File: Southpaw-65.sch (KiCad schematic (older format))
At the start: 14 parts

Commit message: Leftpad and top row added
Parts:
- removed U?: ATmega32U4-AU, Package_QFP:TQFP-44_10x10mm_P0.8mm, symbol MCU_Microchip_ATmega:ATmega32U4-AU
- added C?: 1uF, symbol Device:C_Small
- added D? (x35): SOD-123, symbol Device:D_Small
- added J?: USB_C_Receptacle_USB2.0, symbol Connector:USB_C_Receptacle_USB2.0
- added MX? (x35): MX-NoLED, symbol MX_Alps_Hybrid:MX-NoLED
- added R? (x2): 5k1, symbol Device:R_Small
- added U?: ATmega32U4-AU, Package_QFP:TQFP-44_10x10mm_P0.8mm, symbol MCU_Microchip_ATmega:ATmega32U4-AU
- C?: value C_Small -> 1uF
- C? (x3): value 0.1uF -> 100nF
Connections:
- net +5V: now also C?.1, J?.A4 (VBUS), J?.A9 (VBUS), J?.B4 (VBUS), J?.B9 (VBUS), U?.14 (VCC), U?.2 (UVCC), U?.24 (AVCC), U?.34 (VCC), U?.44 (AVCC), U?.7 (VBUS)
- net D+: now also J?.A6 (D+), J?.B6 (D+)
- net D-: now also J?.A7 (D-), J?.B7 (D-)
- net GND: now also C?.2, J?.A1 (GND), J?.A12 (GND), J?.B1 (GND), J?.B12 (GND), J?.S1 (SHIELD), R?.1, R?.1, U?.15 (GND), U?.23 (GND), U?.35 (GND), U?.43 (GND), U?.5 (UGND)
- net Reset: now reaches R?.2, SW?.2
- net Reset: now also U?.13 (~RESET)
- net C16: now reaches C?.1, Y?.3
- net C16: now also U?.16 (XTAL2)
- net C17: now reaches C?.1, Y?.1
- net C17: now also U?.17 (XTAL1)
- net at R?.1: now also U?.3 (D-)
- net at R?.2: now also U?.33 (~HWB~/PE2)
- net at R?.1: now also U?.4 (D+)
- net at C?.1: now also U?.6 (UCAP)
- new net: J?.A5 (CC1), R?.2
- new net: J?.B5 (CC2), R?.2
- new net: D?.2 (A), MX?.2 (ROW) (x35)
- new net COL0: MX?.1 (COL), MX?.1 (COL), MX?.1 (COL), MX?.1 (COL), MX?.1 (COL)
- new net COL1: MX?.1 (COL), MX?.1 (COL), MX?.1 (COL), MX?.1 (COL), MX?.1 (COL)
- new net COL2: MX?.1 (COL), MX?.1 (COL), MX?.1 (COL), MX?.1 (COL), MX?.1 (COL)
- new net COL3: MX?.1 (COL), MX?.1 (COL), MX?.1 (COL), MX?.1 (COL), MX?.1 (COL)
- new net ROW0: D?.1 (K), D?.1 (K), D?.1 (K), D?.1 (K)
- new net ROW1: D?.1 (K), D?.1 (K), D?.1 (K), D?.1 (K)
- new net ROW2: D?.1 (K), D?.1 (K), D?.1 (K), D?.1 (K)
- new net ROW3: D?.1 (K), D?.1 (K), D?.1 (K), D?.1 (K)
- new net ROW4: D?.1 (K), D?.1 (K), D?.1 (K), D?.1 (K)
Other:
- note added: "Crystal Jade"
- note added: "MCU\n"
- note added: "Reset"
- note added: "USB C"
- moved on the sheet: C?, R?, SW?, Y?

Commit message: Finished switch matrix
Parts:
- removed D?: SOD-123, symbol Device:D_Small
- removed MX?: MX-NoLED, symbol MX_Alps_Hybrid:MX-NoLED
- added D? (x59): SOD-123, symbol Device:D_Small
- added MX? (x59): MX-NoLED, symbol MX_Alps_Hybrid:MX-NoLED
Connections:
- net ROW0: now also D?.1 (K), D?.1 (K), D?.1 (K), D?.1 (K), D?.1 (K), D?.1 (K), D?.1 (K), D?.1 (K), D?.1 (K), D?.1 (K), D?.1 (K), D?.1 (K), D?.1 (K), D?.1 (K), D?.1 (K), D?.1 (K)
- net ROW4: now also D?.1 (K), D?.1 (K), D?.1 (K), D?.1 (K), D?.1 (K), D?.1 (K), D?.1 (K), D?.1 (K), D?.1 (K), D?.1 (K), D?.1 (K)
- net COL4: now reaches MX?.1 (COL)
- net COL4: now also MX?.1 (COL), MX?.1 (COL), MX?.1 (COL), MX?.1 (COL)
- net COL5: now reaches MX?.1 (COL)
- net COL5: now also MX?.1 (COL), MX?.1 (COL), MX?.1 (COL), MX?.1 (COL)
- net COL6: now reaches MX?.1 (COL)
- net COL6: now also MX?.1 (COL), MX?.1 (COL), MX?.1 (COL), MX?.1 (COL)
- net COL7: now reaches MX?.1 (COL)
- net COL7: now also MX?.1 (COL), MX?.1 (COL), MX?.1 (COL)
- net COL8: now reaches MX?.1 (COL)
- net COL8: now also MX?.1 (COL), MX?.1 (COL), MX?.1 (COL), MX?.1 (COL)
- net COL9: now reaches MX?.1 (COL)
- net COL9: now also MX?.1 (COL), MX?.1 (COL), MX?.1 (COL), MX?.1 (COL)
- net COL10: now reaches MX?.1 (COL)
- net COL10: now also MX?.1 (COL), MX?.1 (COL), MX?.1 (COL), MX?.1 (COL)
- net COL11: now reaches MX?.1 (COL)
- net COL11: now also MX?.1 (COL), MX?.1 (COL), MX?.1 (COL)
- net COL12: now reaches MX?.1 (COL)
- net COL12: now also MX?.1 (COL), MX?.1 (COL), MX?.1 (COL)
- net COL13: now reaches MX?.1 (COL)
- net COL13: now also MX?.1 (COL), MX?.1 (COL), MX?.1 (COL), MX?.1 (COL)
- net COL14: now reaches MX?.1 (COL)
- net COL14: now also MX?.1 (COL), MX?.1 (COL), MX?.1 (COL), MX?.1 (COL)
- net COL15: now reaches MX?.1 (COL)
- net COL15: now also MX?.1 (COL), MX?.1 (COL), MX?.1 (COL)
- net COL17: now reaches MX?.1 (COL)
- net COL17: now also MX?.1 (COL)
- net COL18: now reaches MX?.1 (COL)
- net COL18: now also MX?.1 (COL), MX?.1 (COL), MX?.1 (COL)
- new net: D?.2 (A), MX?.2 (ROW) (x59)
- new net: D?.1 (K), D?.1 (K), D?.1 (K), D?.1 (K), D?.1 (K), D?.1 (K), D?.1 (K), D?.1 (K), D?.1 (K), D?.1 (K), D?.1 (K), D?.1 (K), D?.1 (K), D?.1 (K), D?.1 (K), D?.1 (K)
- new net: D?.1 (K), D?.1 (K), D?.1 (K), D?.1 (K), D?.1 (K), D?.1 (K), D?.1 (K), D?.1 (K), D?.1 (K), D?.1 (K), D?.1 (K), D?.1 (K), D?.1 (K), D?.1 (K), D?.1 (K) (x2)
- new net COL16: MX?.1 (COL), MX?.1 (COL), MX?.1 (COL), MX?.1 (COL), MX?.1 (COL)
- new net COL19: MX?.1 (COL), MX?.1 (COL), MX?.1 (COL), MX?.1 (COL)
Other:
- moved on the sheet: D?, MX?

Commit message: Redid matrix
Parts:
- gave numbers to parts that had none: 204
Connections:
- net COL18: now also MX4-18.1 (COL)
- net COL19: now also MX4-19.1 (COL)
- net ROW1: now also D25.1 (K), D26.1 (K), D27.1 (K), D28.1 (K), D29.1 (K), D30.1 (K), D31.1 (K), D32.1 (K), D33.1 (K), D34.1 (K), D35.1 (K), D36.1 (K), D37.1 (K), D38.1 (K), D39.1 (K), D40.1 (K)
- net ROW2: now also D45.1 (K), D46.1 (K), D47.1 (K), D48.1 (K), D49.1 (K), D50.1 (K), D51.1 (K), D52.1 (K), D53.1 (K), D54.1 (K), D55.1 (K), D56.1 (K), D57.1 (K), D58.1 (K), D59.1 (K)
- net ROW3: now also D64.1 (K), D65.1 (K), D66.1 (K), D67.1 (K), D68.1 (K), D69.1 (K), D70.1 (K), D71.1 (K), D72.1 (K), D73.1 (K), D74.1 (K), D75.1 (K), D76.1 (K), D77.1 (K), D78.1 (K)

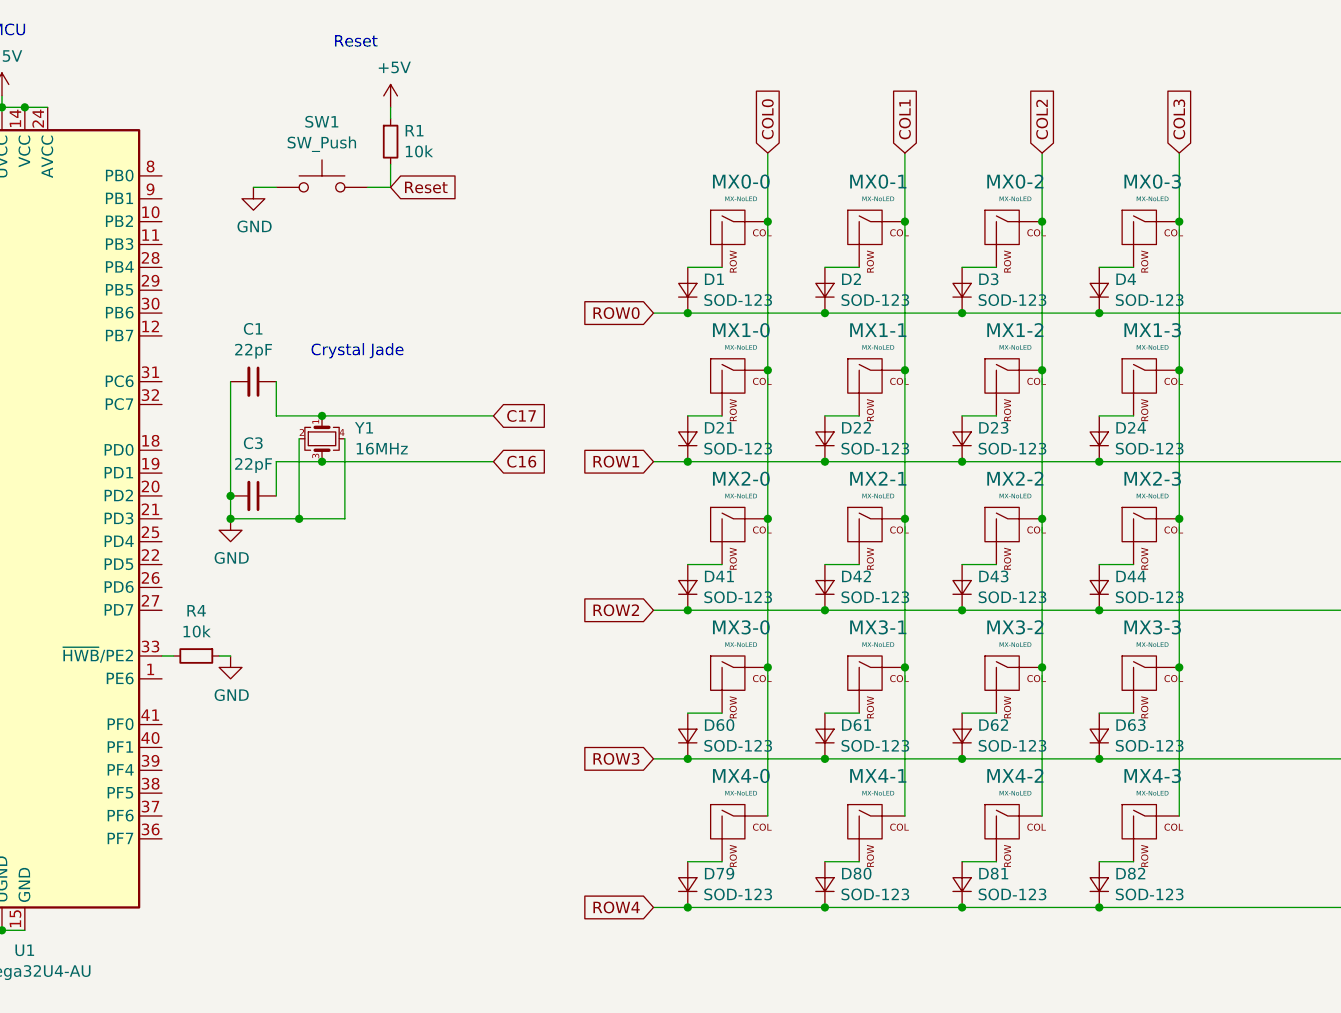
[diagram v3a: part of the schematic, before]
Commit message: Connected Matrix to Atmega
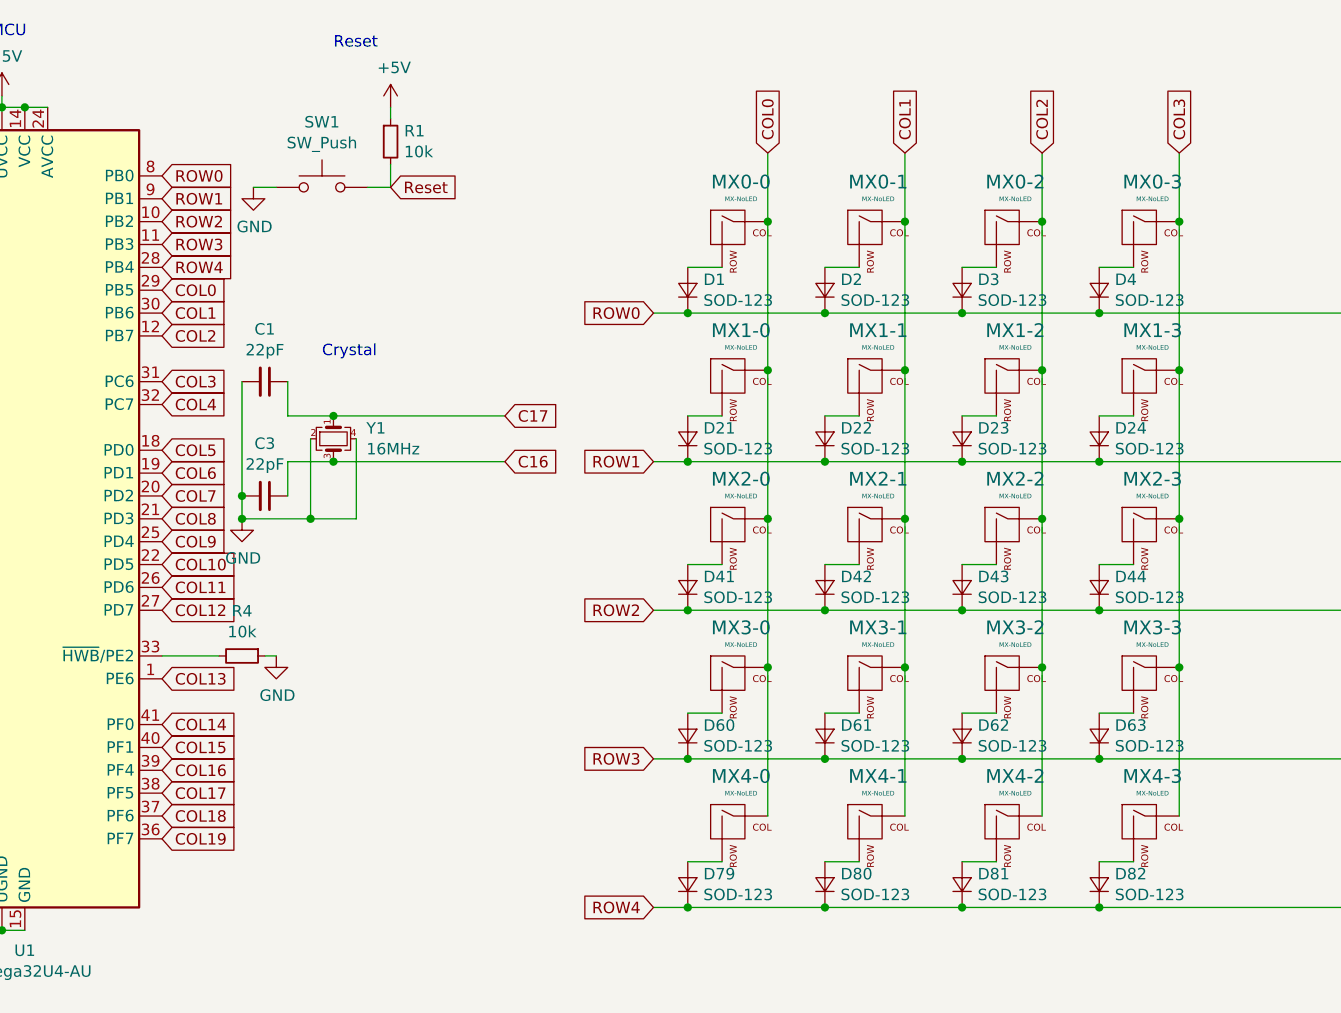
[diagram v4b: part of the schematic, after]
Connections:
- net COL0: now also U1.29 (PB5)
- net COL1: now also U1.30 (PB6)
- net COL10: now also U1.22 (PD5)
- net COL11: now also U1.26 (PD6)
- net COL12: now also U1.27 (PD7)
- net COL13: now also U1.1 (PE6)
- net COL14: now also U1.41 (PF0)
- net COL15: now also U1.40 (PF1)
- net COL16: now also U1.39 (PF4)
- net COL17: now also U1.38 (PF5)
- net COL18: now also U1.37 (PF6)
- net COL19: now also U1.36 (PF7)
- net COL2: now also U1.12 (PB7)
- net COL3: now also U1.31 (PC6)
- net COL4: now also U1.32 (PC7)
- net COL5: now also U1.18 (PD0)
- net COL6: now also U1.19 (PD1)
- net COL7: now also U1.20 (PD2)
- net COL8: now also U1.21 (PD3)
- net COL9: now also U1.25 (PD4)
- net ROW0: now also U1.8 (PB0)
- net ROW1: now also U1.9 (PB1)
- net ROW2: now also U1.10 (PB2)
- net ROW3: now also U1.11 (PB3)
- net ROW4: now also U1.28 (PB4)
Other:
- note added: "Crystal"
- note removed: "Crystal Jade"
- moved on the sheet: C1, C3, R4, Y1

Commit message: Set footprints for everything but switches and capcitators
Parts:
- D1, D10, D11, D12, D13, D14, D15, D16, D17, D18, D19, D2, D20, D21, D22, D23, D24, D25, D26, D27, D28, D29, D3, D30, D31, D32, D33, D34, D35, D36, D37, D38, D39, D4, D40, D41, D42, D43, D44, D45, D46, D47, D48, D49, D5, D50, D51, D52, D53, D54, D55, D56, D57, D58, D59, D6, D60, D61, D62, D63, D64, D65, D66, D67, D68, D69, D7, D70, D71, D72, D73, D74, D75, D76, D77, D78, D79, D8, D80, D81, D82, D83, D84, D85, D86, D87, D88, D89, D9, D90, D91, D92, D93: footprint (none) -> Diode_THT:D_DO-41_SOD81_P7.62mm_Horizontal
- J1: footprint (none) -> Connector_USB:USB_C_Receptacle_GCT_USB4085
- R1, R2, R3, R4, R5, R6: footprint (none) -> Resistor_THT:R_Axial_DIN0207_L6.3mm_D2.5mm_P7.62mm_Horizontal
- SW1: footprint (none) -> random-keyboard-parts:PushButton_6x6mm_TH
- Y1: footprint (none) -> Crystal:Crystal_HC49-U_Vertical

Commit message: Set keys
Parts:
- removed C2: 1uF, symbol Device:C_Small
- removed D57, D76: SOD-123, Diode_THT:D_DO-41_SOD81_P7.62mm_Horizontal, symbol Device:D_Small
- removed MX2-16, MX3-16: MX-NoLED, symbol MX_Alps_Hybrid:MX-NoLED
- removed R4: 10k, Resistor_THT:R_Axial_DIN0207_L6.3mm_D2.5mm_P7.62mm_Horizontal, symbol Device:R_Small
- removed U1: ATmega32U4-AU, Package_QFP:TQFP-44_10x10mm_P0.8mm, symbol MCU_Microchip_ATmega:ATmega32U4-AU
- added U1: ATmega32A-PU, Package_DIP:DIP-40_W15.24mm, symbol MCU_Microchip_ATmega:ATmega32A-PU
- MX0-0, MX0-1, MX0-10, MX0-11, MX0-12, MX0-13, MX0-14, MX0-15, MX0-16, MX0-17, MX0-18, MX0-19, MX0-2, MX0-3, MX0-4, MX0-5, MX0-6, MX0-7, MX0-8, MX0-9, MX1-0, MX1-1, MX1-10, MX1-11, MX1-12, MX1-13, MX1-14, MX1-15, MX1-16, MX1-17, MX1-19, MX1-2, MX1-3, MX1-5, MX1-6, MX1-7, MX1-8, MX1-9, MX2-0, MX2-1, MX2-10, MX2-11, MX2-12, MX2-13, MX2-14, MX2-15, MX2-19, MX2-2, MX2-3, MX2-5, MX2-6, MX2-7, MX2-8, MX2-9, MX3-0, MX3-1, MX3-10, MX3-11, MX3-12, MX3-13, MX3-14, MX3-18, MX3-19, MX3-2, MX3-3, MX3-5, MX3-6, MX3-7, MX3-8, MX3-9, MX4-0, MX4-1, MX4-14, MX4-16, MX4-18, MX4-19, MX4-2, MX4-3, MX4-5, MX4-9: footprint (none) -> MX_Alps_Hybrid:MX-1U
- MX1-18, MX1-4, MX4-4, MX4-6: footprint (none) -> MX_Alps_Hybrid:MX-1.5U
- MX2-18, MX3-4: footprint (none) -> MX_Alps_Hybrid:MX-2.25U
- MX2-4, MX3-15: footprint (none) -> MX_Alps_Hybrid:MX-1.75U
- MX4-10, MX4-8: footprint (none) -> MX_Alps_Hybrid:MX-2.75U
- MX4-13: footprint (none) -> MX_Alps_Hybrid:MX-1.25U
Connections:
- net +5V: now also U1.10 (VCC), U1.30 (AVCC)
- net C16: now also U1.12 (XTAL2)
- net C17: now also U1.13 (XTAL1)
- net COL0: now also U1.35 (PA5)
- net COL1: now also U1.34 (PA6)
- net COL10: now also U1.8 (PB7)
- net COL11: now also U1.22 (PC0)
- net COL12: now also U1.23 (PC1)
- net COL13: now also U1.24 (PC2)
- net COL14: now also U1.25 (PC3)
- net COL15: now also U1.26 (PC4)
- net COL16: now also U1.27 (PC5)
- net COL17: now also U1.28 (PC6)
- net COL18: now also U1.29 (PC7)
- net COL19: now also U1.14 (PD0)
- net COL2: now also U1.33 (PA7)
- net COL3: now also U1.1 (PB0)
- net COL4: now also U1.2 (PB1)
- net COL5: now also U1.3 (PB2)
- net COL6: now also U1.4 (PB3)
- net COL7: now also U1.5 (PB4)
- net COL8: now also U1.6 (PB5)
- net COL9: now also U1.7 (PB6)
- net D+: now also R3.1; no longer R2.2
- net D-: now also R2.1; no longer R3.2
- net GND: now also U1.11 (GND), U1.31 (GND)
- net ROW0: now also U1.40 (PA0)
- net ROW1: now also U1.39 (PA1)
- net ROW2: now also U1.38 (PA2)
- net ROW3: now also U1.37 (PA3)
- net ROW4: now also U1.36 (PA4)
- net Reset: now also U1.9 (~RESET)
- new net: R2.2, U1.16 (PD2)
- new net: R3.2, U1.17 (PD3)
- no-connect marks 0 -> 5
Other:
- note removed: "MCU\n"
- moved on the sheet: C1, C3, R1, SW1, Y1

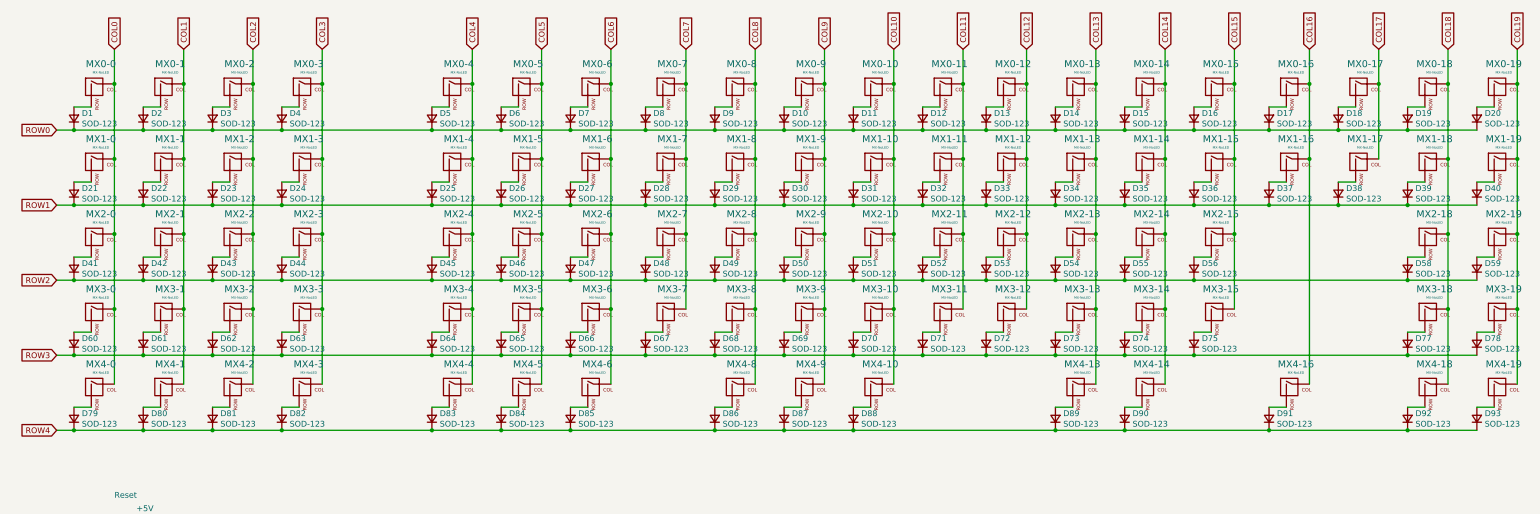
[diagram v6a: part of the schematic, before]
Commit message: Labeled the Diodes and reorganized the layout
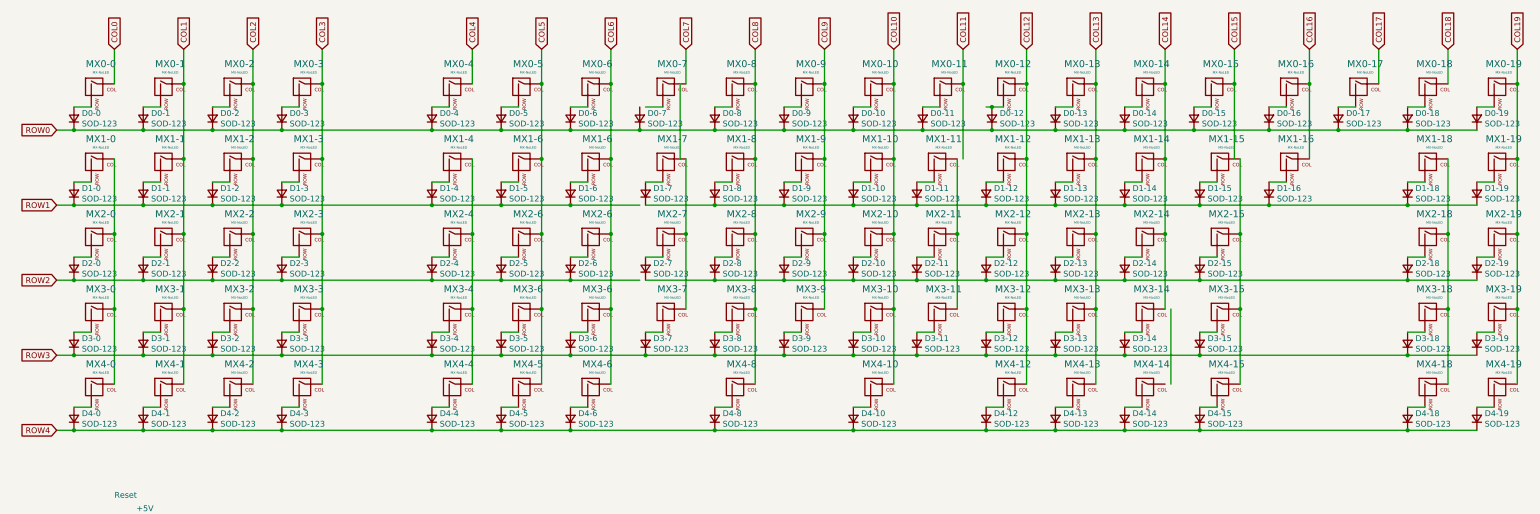
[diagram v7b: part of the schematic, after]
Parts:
- removed D20, D26, D4, D46, D65: SOD-123, Diode_THT:D_DO-41_SOD81_P7.62mm_Horizontal, symbol Device:D_Small
- removed MX1-5, MX2-5, MX3-5: MX-NoLED, MX_Alps_Hybrid:MX-1U, symbol MX_Alps_Hybrid:MX-NoLED
- added D0-0, D0-4, D2-15, D3-15: SOD-123, Diode_THT:D_DO-41_SOD81_P7.62mm_Horizontal, symbol Device:D_Small
- added MX2-15: MX-NoLED, MX_Alps_Hybrid:MX-1U, symbol MX_Alps_Hybrid:MX-NoLED
- added MX3-15: MX-NoLED, MX_Alps_Hybrid:MX-1.75U, symbol MX_Alps_Hybrid:MX-NoLED
- MX3-14: renamed from MX3-15; footprint MX_Alps_Hybrid:MX-1.75U -> MX_Alps_Hybrid:MX-1U
- MX4-12: renamed from MX4-10; footprint MX_Alps_Hybrid:MX-2.75U -> MX_Alps_Hybrid:MX-3U
- MX4-6: footprint MX_Alps_Hybrid:MX-1.5U -> MX_Alps_Hybrid:MX-1.25U
- MX4-8: footprint MX_Alps_Hybrid:MX-2.75U -> MX_Alps_Hybrid:MX-3U
- renumbered D1 to D0-1, D10 to D0-10, D11 to D0-11, D12 to D0-12, D13 to D0-13, D14 to D0-14, D15 to D0-15, D16 to D0-16, D17 to D0-17, D18 to D0-18, D19 to D0-19, D2 to D0-2, D3 to D0-3, D5 to D0-5, D6 to D0-6, D7 to D0-7, D8 to D0-8, D9 to D0-9, D21 to D1-0, D22 to D1-1, D32 to D1-10, D33 to D1-11, D34 to D1-12, D35 to D1-13, D36 to D1-14, D37 to D1-15, D38 to D1-16, D39 to D1-18, D40 to D1-19, D23 to D1-2, D24 to D1-3, D25 to D1-4, D27 to D1-5, D28 to D1-6, D29 to D1-7, D30 to D1-8, D31 to D1-9, D41 to D2-0, D42 to D2-1, D52 to D2-10, D53 to D2-11, D54 to D2-12, D55 to D2-13, D56 to D2-14, D58 to D2-18, D59 to D2-19, D43 to D2-2, D44 to D2-3, D45 to D2-4, D47 to D2-5, D48 to D2-6, D49 to D2-7, D50 to D2-8, D51 to D2-9, D60 to D3-0, D61 to D3-1, D71 to D3-10, D72 to D3-11, D73 to D3-12, D74 to D3-13, D75 to D3-14, D77 to D3-18, D78 to D3-19, D62 to D3-2, D63 to D3-3, D64 to D3-4, D66 to D3-5, D67 to D3-6, D68 to D3-7, D69 to D3-8, D70 to D3-9, D79 to D4-0, D80 to D4-1, D87 to D4-10, D88 to D4-12, D89 to D4-13, D90 to D4-14, D91 to D4-15, D92 to D4-18, D93 to D4-19, D81 to D4-2, D82 to D4-3, D83 to D4-4, D84 to D4-5, D85 to D4-6, D86 to D4-8, MX1-11 to MX1-10, MX1-12 to MX1-11, MX1-13 to MX1-12, MX1-14 to MX1-13, MX1-15 to MX1-14, MX1-16 to MX1-15, MX1-17 to MX1-16, MX1-7 to MX1-6, MX1-8 to MX1-7, MX1-9 to MX1-8, MX1-10 to MX1-9, MX2-11 to MX2-10, MX2-12 to MX2-11, MX2-13 to MX2-12, MX2-14 to MX2-13, MX2-15 to MX2-14, MX2-7 to MX2-6, MX2-8 to MX2-7, MX2-9 to MX2-8, MX2-10 to MX2-9, MX3-11 to MX3-10, MX3-12 to MX3-11, MX3-13 to MX3-12, MX3-14 to MX3-13, MX3-7 to MX3-6, MX3-8 to MX3-7, MX3-9 to MX3-8, MX3-10 to MX3-9, MX4-9 to MX4-10, MX4-16 to MX4-15
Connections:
- wire segments 319 -> 314
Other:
- moved on the sheet: D0-1, D0-10, D0-11, D0-12, D0-13, D0-14, D0-15, D0-16, D0-17, D0-18, D0-19, D0-2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

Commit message: Backup #2
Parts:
- renumbered MX1-6 to MX1-5, MX2-6 to MX2-5, MX3-6 to MX3-5
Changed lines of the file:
@@
 Connection ~ 8600 1800
 $Comp
-L MX_Alps_Hybrid:MX-NoLED MX2-6
+L MX_Alps_Hybrid:MX-NoLED MX2-5
 U 1 1 5FAD7A4B
 P 8800 2750
-F 0 "MX2-6" H 8833 2973 60  0000 C CNN
+F 0 "MX2-5" H 8833 2973 60  0000 C CNN
 F 1 "MX-NoLED" H 8833 2899 20  0000 C CNN
 F 2 "MX_Alps_Hybrid:MX-1U" H 8175 2725 60  0001 C CNN
@@
 $EndComp
 $Comp
-L MX_Alps_Hybrid:MX-NoLED MX3-6
+L MX_Alps_Hybrid:MX-NoLED MX3-5
 U 1 1 60263F68
 P 8800 3400
-F 0 "MX3-6" H 8833 3623 60  0000 C CNN
+F 0 "MX3-5" H 8833 3623 60  0000 C CNN
 F 1 "MX-NoLED" H 8833 3549 20  0000 C CNN
 F 2 "MX_Alps_Hybrid:MX-1U" H 8175 3375 60  0001 C CNN
@@
 	8750 2250 8600 2250
 $Comp
-L MX_Alps_Hybrid:MX-NoLED MX1-6
+L MX_Alps_Hybrid:MX-NoLED MX1-5
 U 1 1 5FAA0AE5
 P 8800 2100
-F 0 "MX1-6" H 8833 2323 60  0000 C CNN
+F 0 "MX1-5" H 8833 2323 60  0000 C CNN
 F 1 "MX-NoLED" H 8833 2249 20  0000 C CNN
 F 2 "MX_Alps_Hybrid:MX-1U" H 8175 2075 60  0001 C CNN
